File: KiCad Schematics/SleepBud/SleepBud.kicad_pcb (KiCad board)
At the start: 2 copper layers, 165 x 55 mm, 106 parts, among them J1 12V Barrel Jack, J2 USB_B_Micro, J3 Button Connector, J4 AM312 Connector, J5 LED Lamp Connector, J6 Connector to Buzzer, Q1 DMG3415U-7, Q2 AO3400A, SW1 EN Button, SW2 Reset Button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

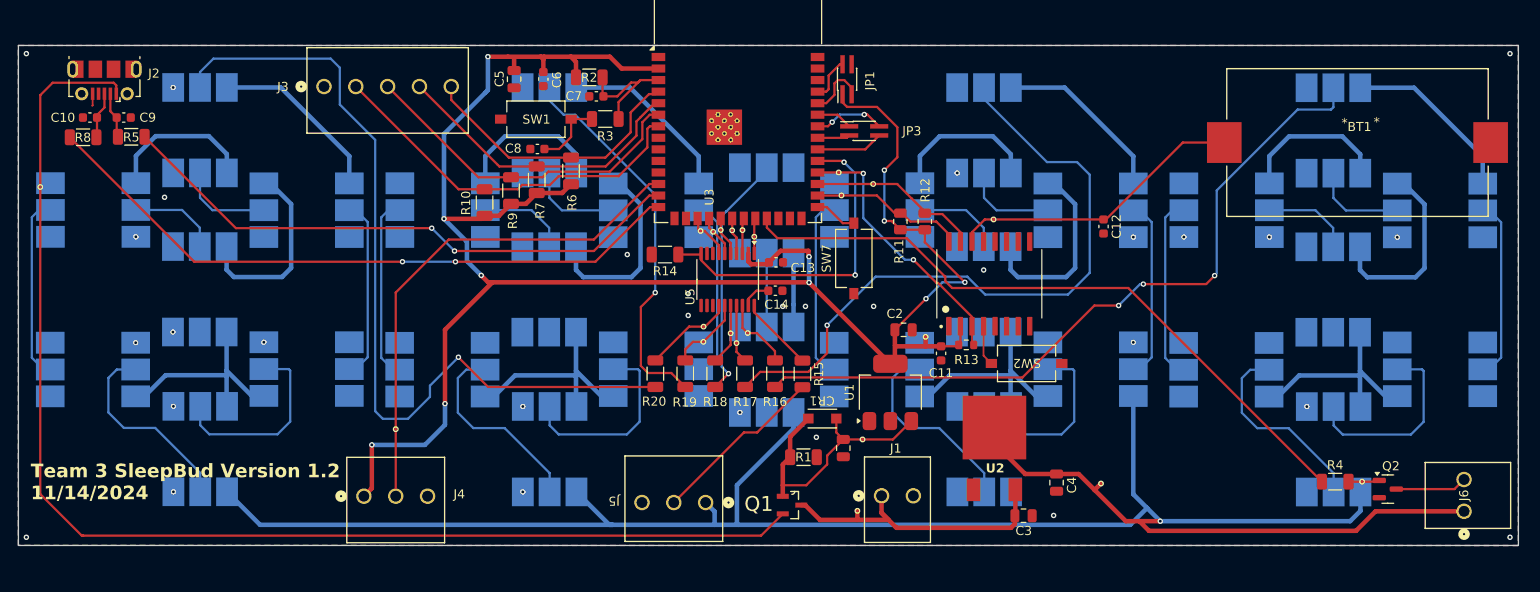
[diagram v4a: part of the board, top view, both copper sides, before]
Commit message: Finished PCB V1.5
Added LEDs to see if PCB is getting power

Changed TestPoint sizes

Added more grounds to even out board
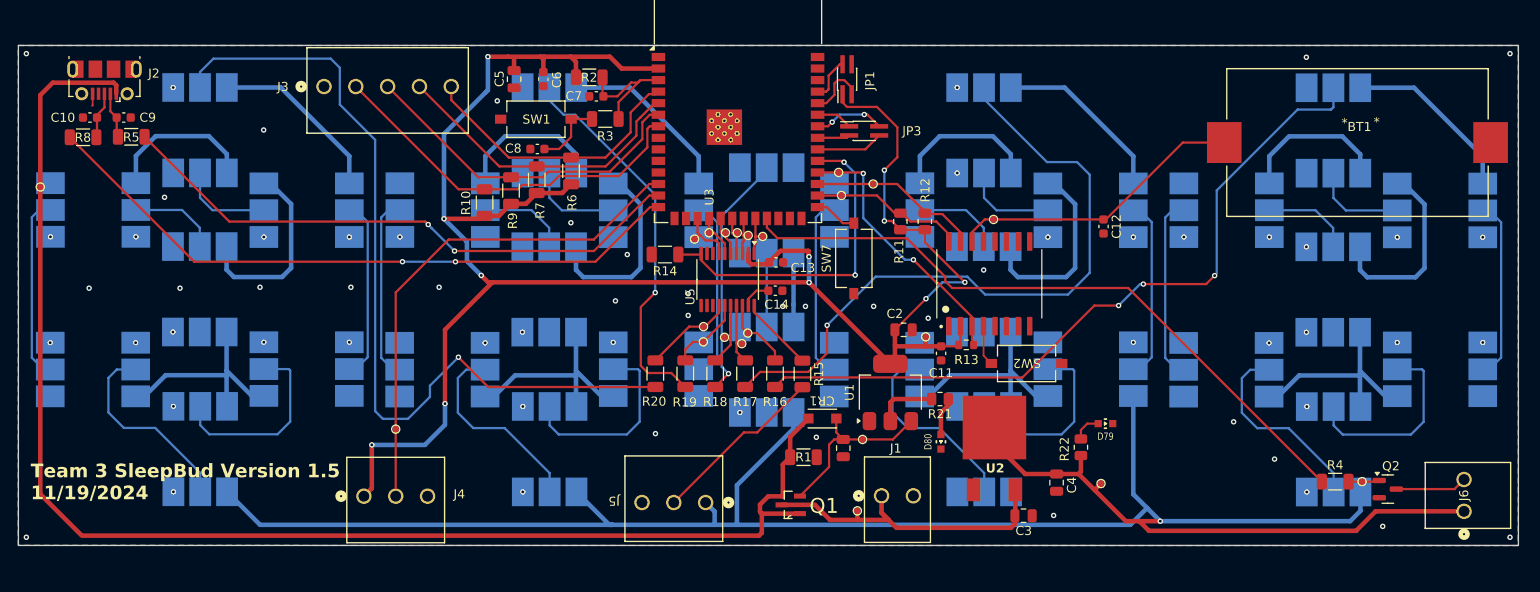
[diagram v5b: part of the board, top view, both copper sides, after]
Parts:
- added D79: WL-SMCW_0603, 150060RS75000:WL-SMCW_0603, F.Cu at (176.7, 95.6)
- added D80: WL-SMCW_0603, 150060RS75000:WL-SMCW_0603, F.Cu at (158.6, 97.6)
- added R21: 100, Resistor_SMD:R_0805_2012Metric, F.Cu at (158.5, 92.9)
- added R22: 180, Resistor_SMD:R_0805_2012Metric, F.Cu at (174.0, 98.2)
- moved TP21 1.11 mm to (131.6, 77.7)
- moved TP16 0.93 mm to (139.1, 77.4)
- moved TP17 0.86 mm to (137.5, 77.2)
- moved TP3 0.80 mm to (134.9, 88.5)
- moved TP18 0.62 mm to (136.3, 77.0)
- moved TP19 0.60 mm to (135.0, 77.0)
- moved TP4 0.58 mm to (136.8, 89.2)
- moved TP20 0.46 mm to (133.2, 77.0)
- moved Q1 0.14 mm to (142.1, 104.5), turned to 180 degrees
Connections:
- C1 pad 1: VBUS -> Net-(Q1-S)
- CR1 pad 1: VBUS -> Net-(Q1-S)
- Q1 pad 2: VBUS -> Net-(Q1-S)
- TP9 pad 1: VBUS -> Net-(Q1-S)
- U1 pad 3: VBUS -> Net-(Q1-S)
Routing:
- net Net-(Q1-S): track 0.00 -> 19.7 mm
- net VBUS: track 168.6 -> 155.5 mm
- net +3.3V: track 218.5 -> 225.2 mm
- net Net-(D80-Pad2): track 0.00 -> 4.24 mm
- net Net-(D79-Pad2): track 0.00 -> 3.18 mm
- net +12V: track 33.5 -> 35.7 mm
- net +5V: track 568.2 -> 570.3 mm
- net /IO9 - A6: track 5.08 -> 7.16 mm
- net /IO14 - A1: track 4.06 -> 4.89 mm
- net /B4 - Colon: track 6.74 -> 7.45 mm
- net /B3 - Digit 2: track 6.43 -> 7.03 mm
- net /IO13 - A2: track 4.12 -> 4.62 mm
- net GND: vias 31 -> 64
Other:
- board text added: "Team 3 SleepBud Version 1.5 11/19/2024"
- board text removed: "Team 3 SleepBud Version 1.2 11/14/2024"

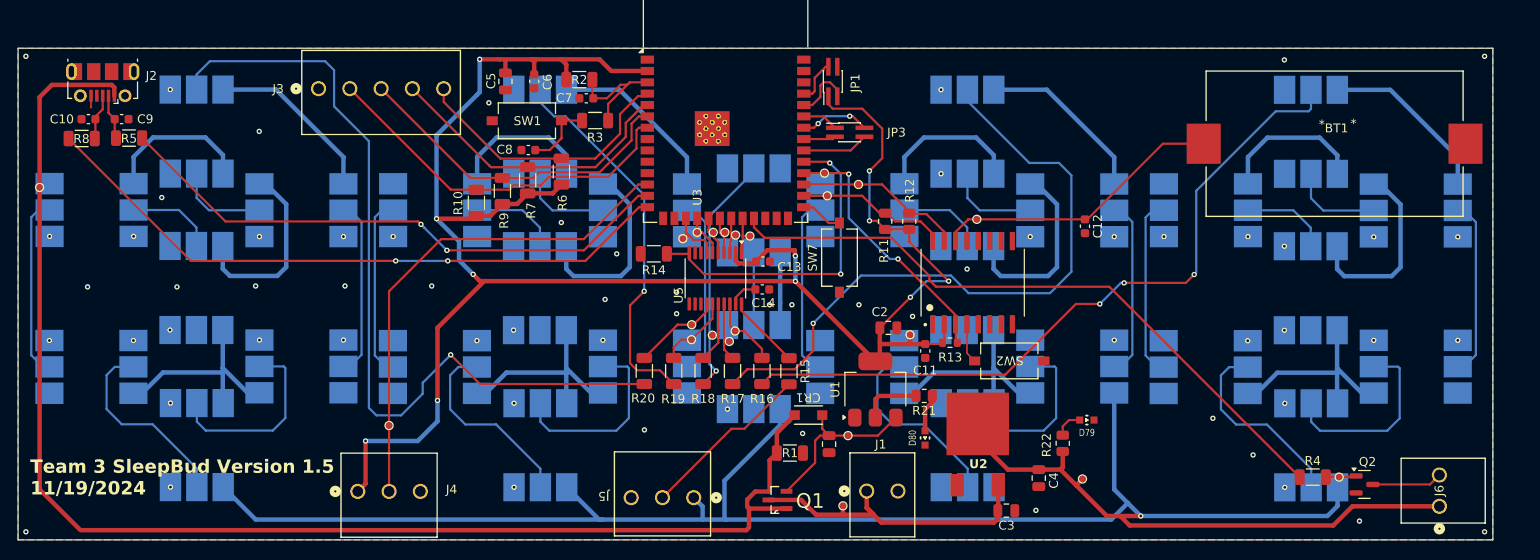
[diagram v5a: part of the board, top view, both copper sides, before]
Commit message: Added more grounds vias based off video
also created new gerber files
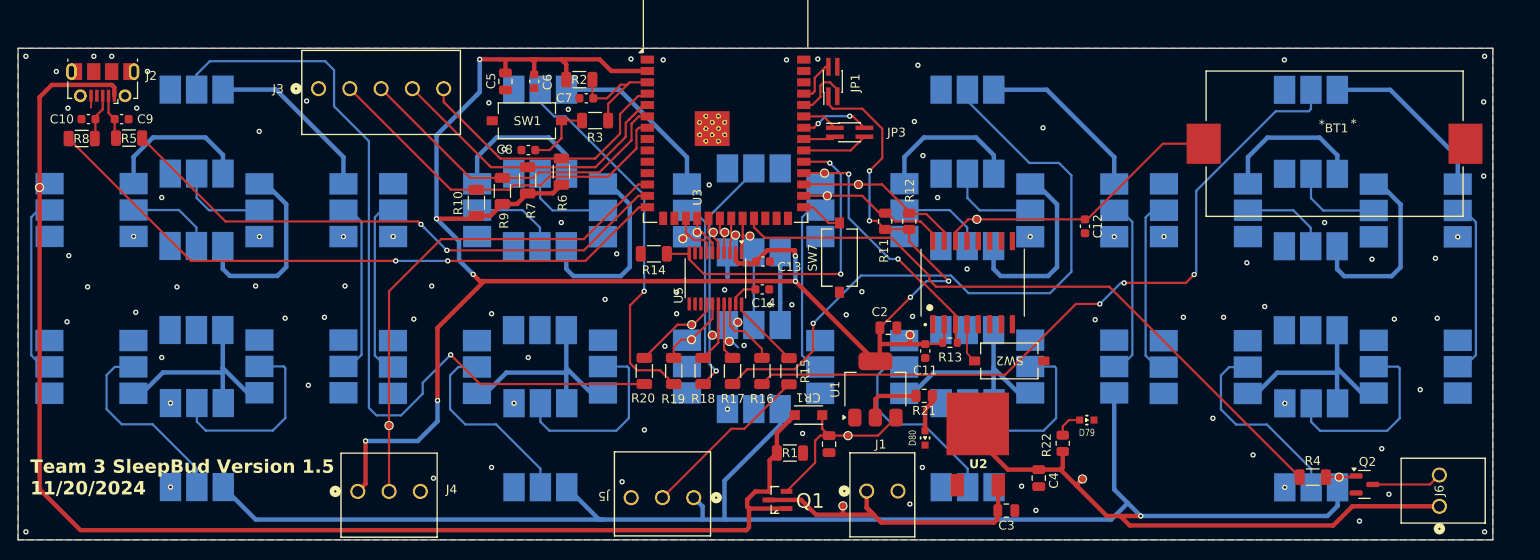
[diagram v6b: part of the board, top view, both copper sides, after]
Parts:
- moved TP5 1.03 mm to (137.8, 87.0)
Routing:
- net GND: track 1.35 -> 7.10 mm, vias 64 -> 97
- net /B2 - Digit 1: track 8.11 -> 9.11 mm
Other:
- board text added: "Team 3 SleepBud Version 1.5 11/20/2024"
- board text removed: "Team 3 SleepBud Version 1.5 11/19/2024"

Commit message: Final PCB
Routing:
- net +5V: track 570.3 -> 943.9 mm, vias 1 -> 5
- net +3.3V: track 225.2 -> 234.1 mm, vias 11 -> 13
- net Net-(D25-DOUT): track 20.0 -> 25.5 mm
- net Net-(D10-DIN): track 20.0 -> 23.5 mm
- net Net-(U3-EN): track 14.7 -> 11.9 mm
- net Net-(D27-DOUT): track 22.1 -> 20.1 mm
- net +12V: track 35.7 -> 34.3 mm
- net GND: track 7.10 -> 5.75 mm, vias 97 -> 114
- net Net-(D28-DOUT): track 20.4 -> 21.7 mm
- net Net-(D18-DOUT): track 20.0 -> 21.1 mm
- net Net-(D2-DOUT): track 20.0 -> 21.1 mm
- net Net-(D5-DOUT): track 20.4 -> 21.4 mm
- net Net-(D21-DOUT): track 20.4 -> 21.3 mm
- net Net-(JP3-TCK): track 7.41 -> 8.03 mm
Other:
- board text added: "11/20/2024"
- board text added: "Team 3 SleepBud Version 1.5"
- board text removed: "11/14/2024"
- board text removed: "Team 3 SleepBud Version 1.1"

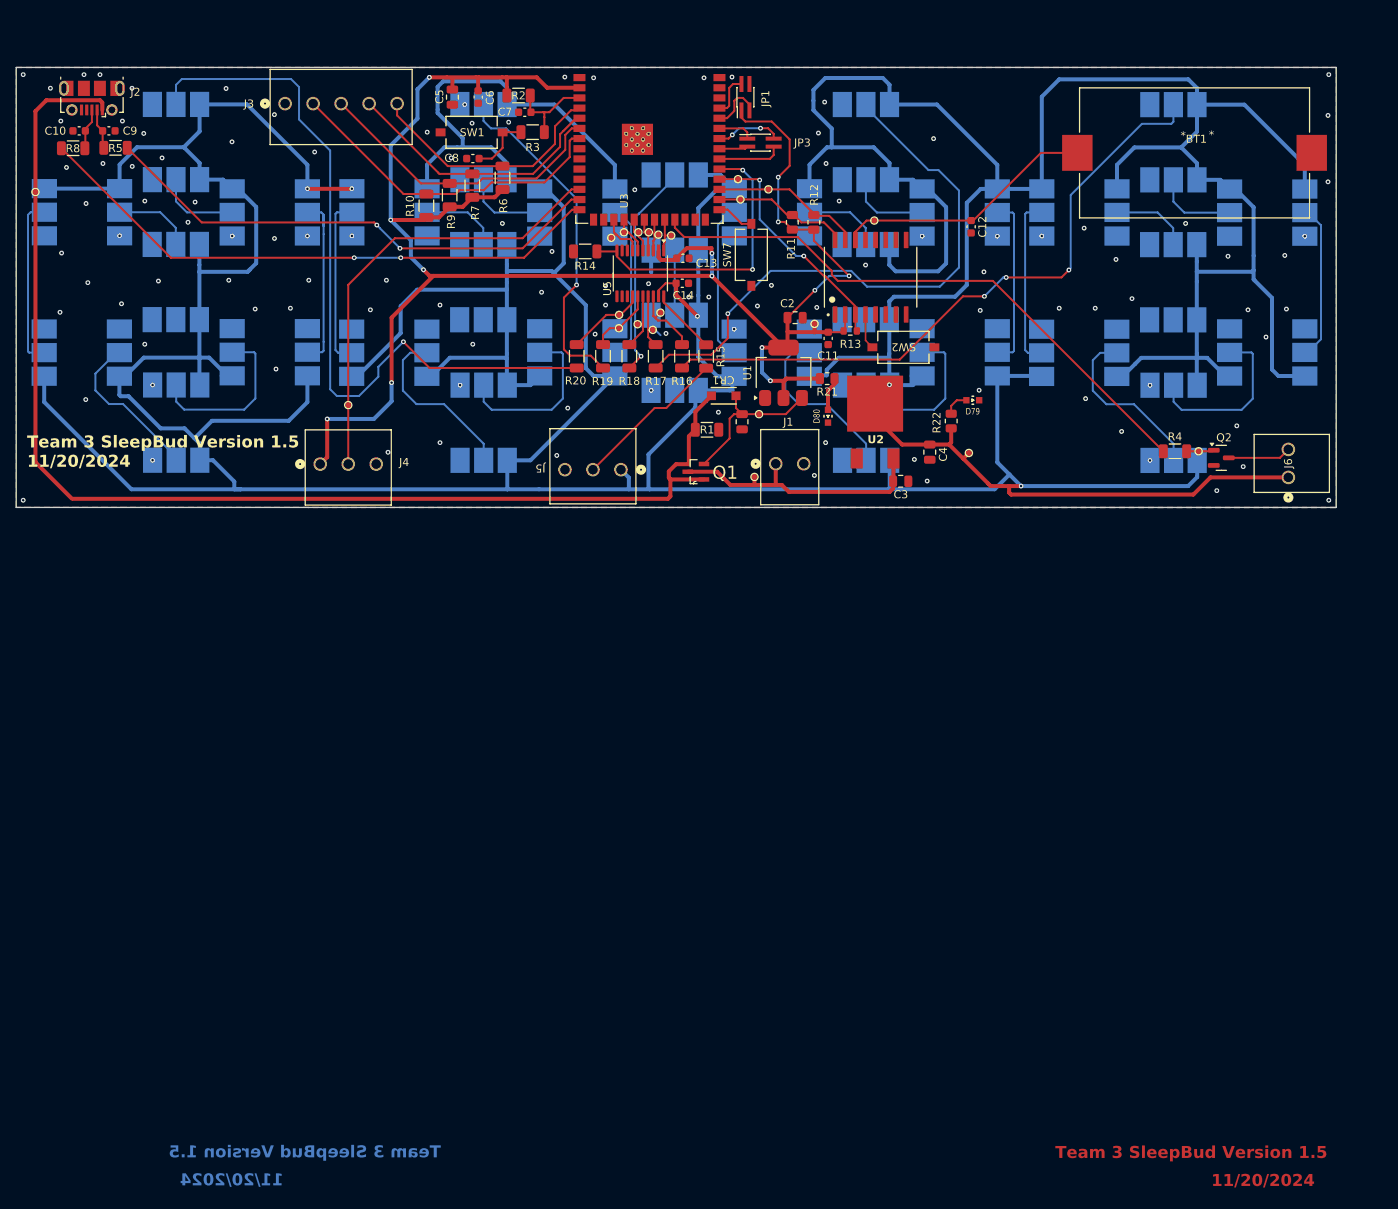
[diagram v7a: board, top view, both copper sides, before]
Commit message: 1.6 Final version of both schematic and pcb
This is the final version. Includes the change from 12V to 5V power supply, resistor values changed to the audio module and esthetical changes to the schematic including resizing of page and rewiring to the 7 segment module
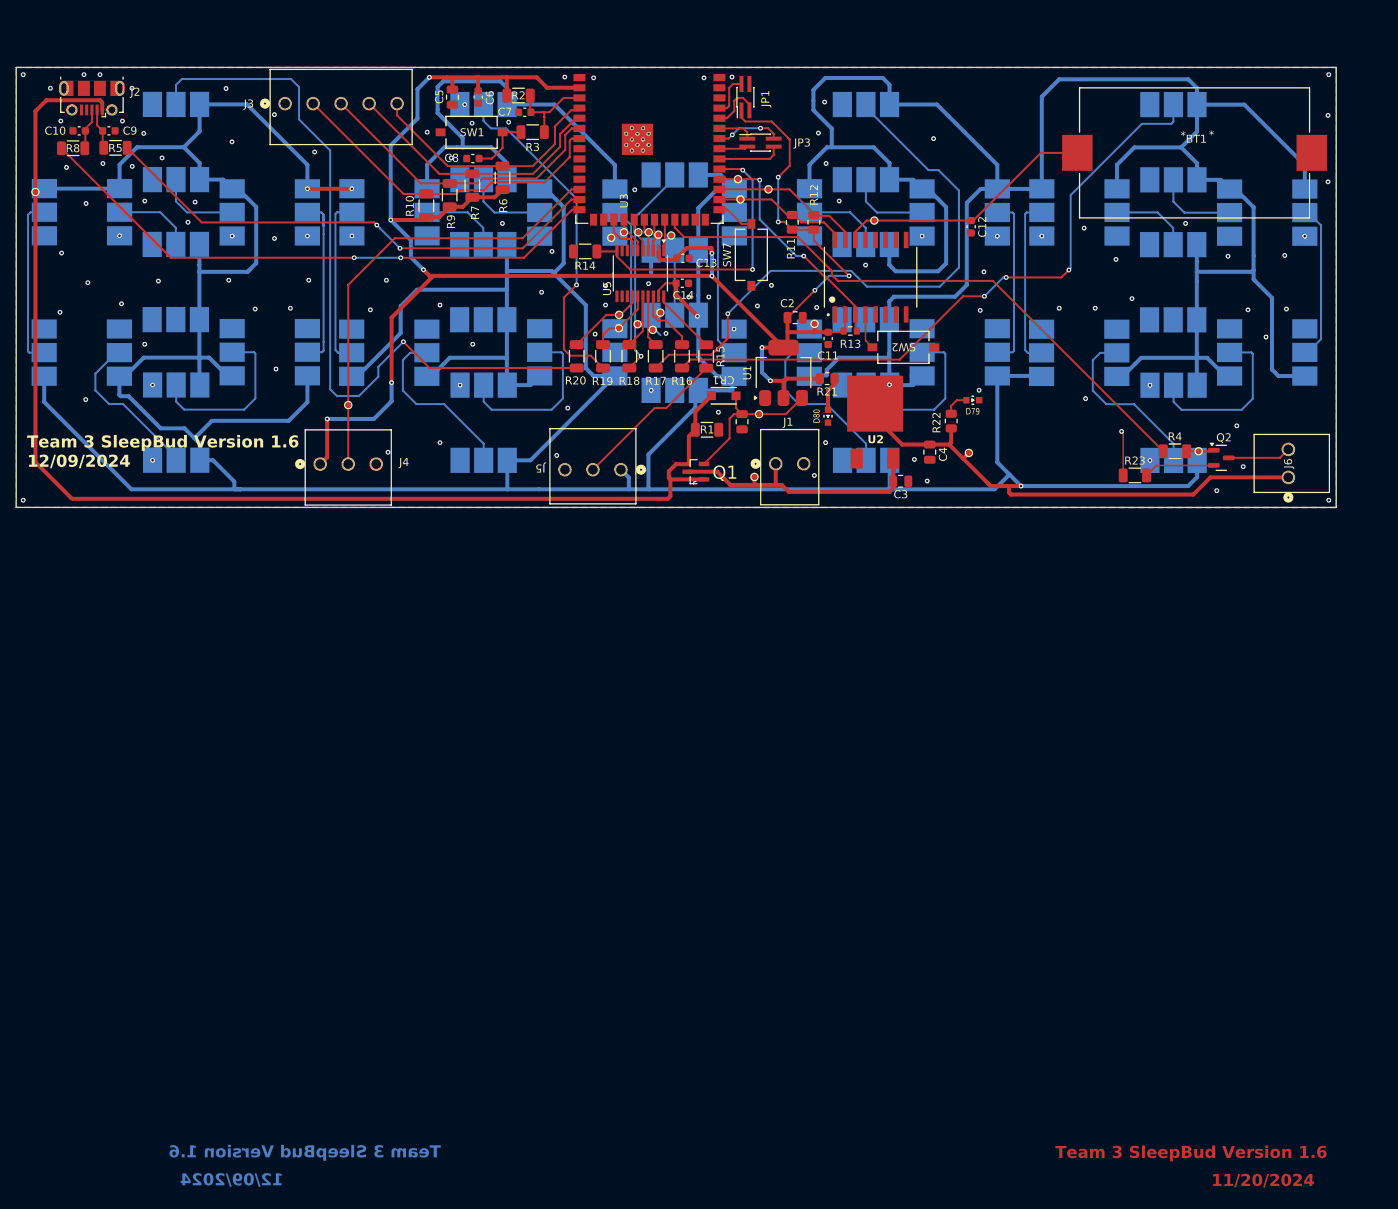
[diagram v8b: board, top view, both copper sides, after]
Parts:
- added R23: 10k, Resistor_SMD:R_1206_3216Metric, F.Cu at (197.0, 105.0)
- R4: value 10k -> 470
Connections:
- Q2 pad 2: GND -> Net-(Q2-S)
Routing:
- net Net-(Q2-S): track 0.00 -> 8.91 mm
- net GND: track 5.75 -> 11.3 mm
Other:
- board text added: "12/09/2024"
- board text added: "Team 3 SleepBud Version 1.6"
- board text added: "Team 3 SleepBud Version 1.6 12/09/2024"
- board text removed: "Team 3 SleepBud Version 1.5"
- board text removed: "Team 3 SleepBud Version 1.5 11/20/2024"
